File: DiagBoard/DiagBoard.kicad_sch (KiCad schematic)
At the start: 64 parts, among them J1 B1, P1 Conn_02x36_Top_Bottom, SW1 SW_DIP_x07, SW2 SW_Push, SW3 SW_DIP_x04

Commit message: DiagBoard: Elements placement
Starting PCB preliminary routing, evaluated elements placement.
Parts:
- removed C1: C, Capacitor_THT:C_Disc_D4.3mm_W1.9mm_P5.00mm, symbol Device:C
- removed SW2: SW_Push, symbol Switch:SW_Push
- removed U_B1: 74LS38, Package_DIP:DIP-14_W7.62mm, symbol 74xx:74LS38
- added C1: 150 uF 15V, Capacitor_THT:CP_Axial_L10.0mm_D4.5mm_P15.00mm_Horizontal, symbol Device:C_Polarized
- added SW2: SW_Push_DPDT, Button_Switch_THT:SW_Push_2P2T_Toggle_CK_PVA2OAH5xxxxxxV2, symbol Switch:SW_Push_DPDT
- added unit 5 of U_AB1
- C2, C3: footprint Capacitor_THT:CP_Axial_L20.0mm_D10.0mm_P26.00mm_Horizontal -> Capacitor_THT:CP_Axial_L25.0mm_D10.0mm_P30.00mm_Horizontal
- D1: footprint Diode_THT:D_5KPW_P12.70mm_Horizontal -> Diode_THT:D_5W_P10.16mm_Horizontal
- DIS1, DIS2: footprint Package_DIP:DIP-14_W7.62mm -> Package_DIP:DIP-14_W7.62mm_Socket
- R5, R6, R7: footprint (none) -> Resistor_THT:R_Axial_DIN0207_L6.3mm_D2.5mm_P10.16mm_Horizontal
- R8: footprint Resistor_THT:R_Axial_DIN0204_L3.6mm_D1.6mm_P5.08mm_Horizontal -> Resistor_THT:R_Axial_DIN0207_L6.3mm_D2.5mm_P10.16mm_Horizontal
- SW1: footprint (none) -> Button_Switch_THT:SW_DIP_SPSTx07_Piano_10.8x19.34mm_W7.62mm_P2.54mm
- SW3: footprint (none) -> Button_Switch_THT:SW_DIP_SPSTx04_Slide_9.78x12.34mm_W7.62mm_P2.54mm
- U_D2, U_E2: footprint (none) -> Package_DIP:DIP-14_W7.62mm
- U_E1: footprint Package_DIP:DIP-12_W7.62mm -> Package_DIP:DIP-16_W7.62mm
- U_F7, U_F8: footprint Package_DIP:DIP-16_W7.62mm -> Package_DIP:DIP-18_W7.62mm
- renumbered U_8A2 to U_A2, U_8A4 to U_A4, U_8A5 to U_A5, U_8A6 to U_A6, U_8B3 to U_B3
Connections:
- net +5V: now also U_AB1.14 (VCC)
- net GND: now also U_A6.1 (OEa), C1.2, SW2.1 (A), SW2.3 (C), U_AB1.7 (GND)
- net at D1.2 (A), RN2.3 (R2), U_C4.1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: now also C1.1, SW2.2 (B)
- no-connect marks 58 -> 61
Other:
- moved on the sheet: U_C4E, U_D1G

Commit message: DiagBoard: Fix messed up address line
A11+A14, A12+A13
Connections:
- net A11: no longer U_B3.5 (O2b), U_E1.12, U_E3.5 (E2), U_E4.6 (E3)
- net A12: no longer U_B3.3 (O3b), U_E1.10, U_E3.3 (A2), U_E4.3 (A2)
- new net A13: U_B3.3 (O3b), U_E1.10, U_E3.3 (A2), U_E4.3 (A2)
- new net A14: U_B3.5 (O2b), U_E1.12, U_E3.5 (E2), U_E4.6 (E3)
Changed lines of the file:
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@@
 		)
 	)
-	(label "A13"
+	(label "A12"
 		(at 577.85 198.12 0)
 		(fields_autoplaced yes)
@@
 		)
 	)
-	(label "A14"
+	(label "A11"
 		(at 577.85 195.58 0)
 		(fields_autoplaced yes)
@@
 		)
 	)
-	(label "A11"
+	(label "A14"
 		(at 577.85 203.2 0)
 		(fields_autoplaced yes)
@@
 		)
 	)
-	(label "A12"
+	(label "A13"
 		(at 577.85 200.66 0)
 		(fields_autoplaced yes)

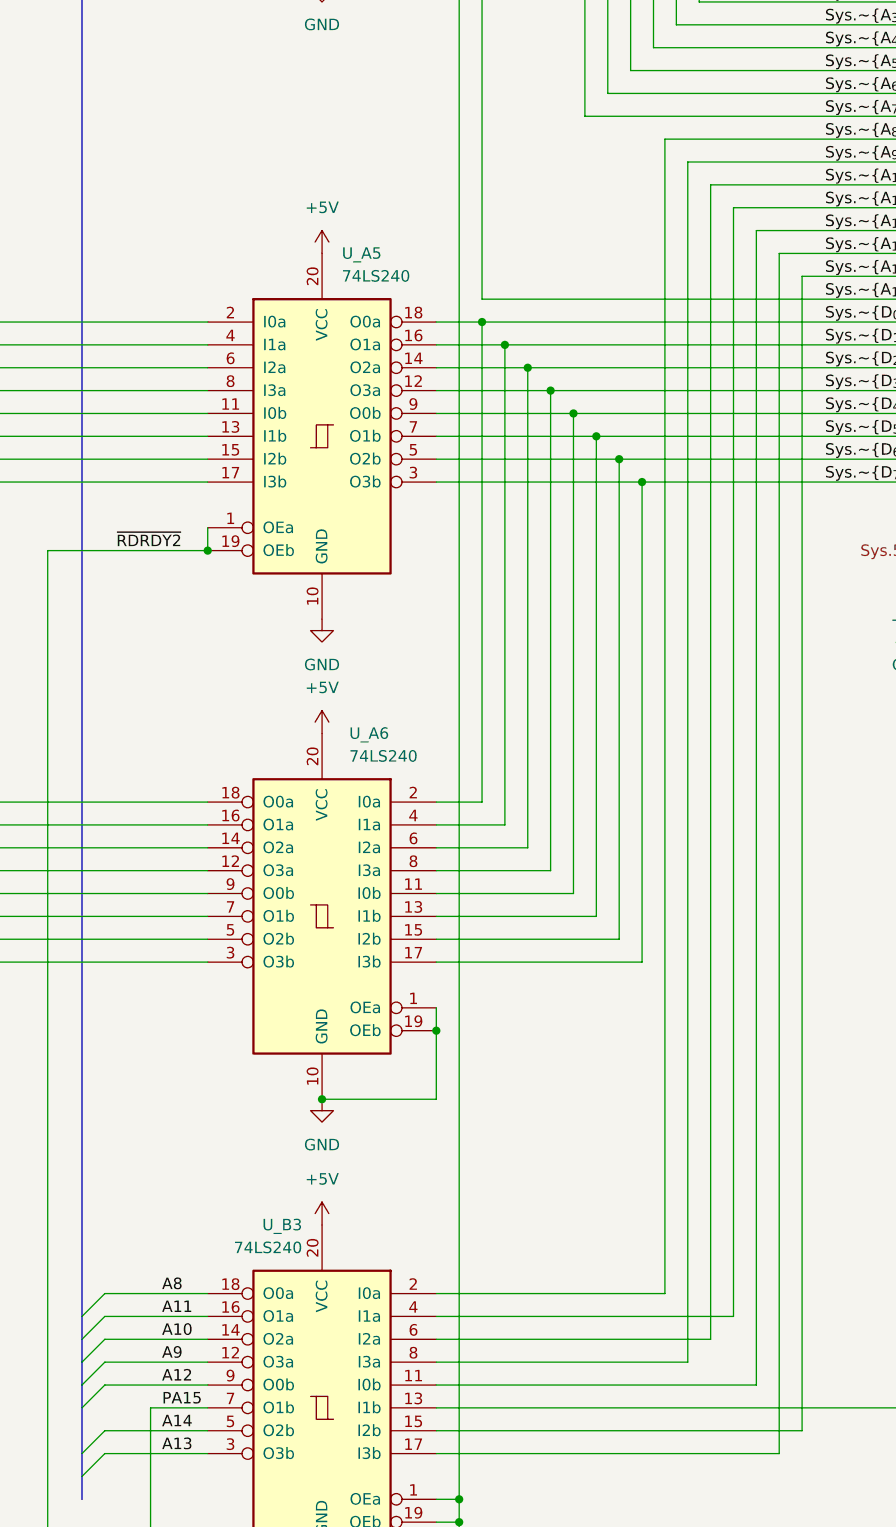
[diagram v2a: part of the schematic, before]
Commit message: DiagBoard: Untwist U_B3 lines
Routes easier
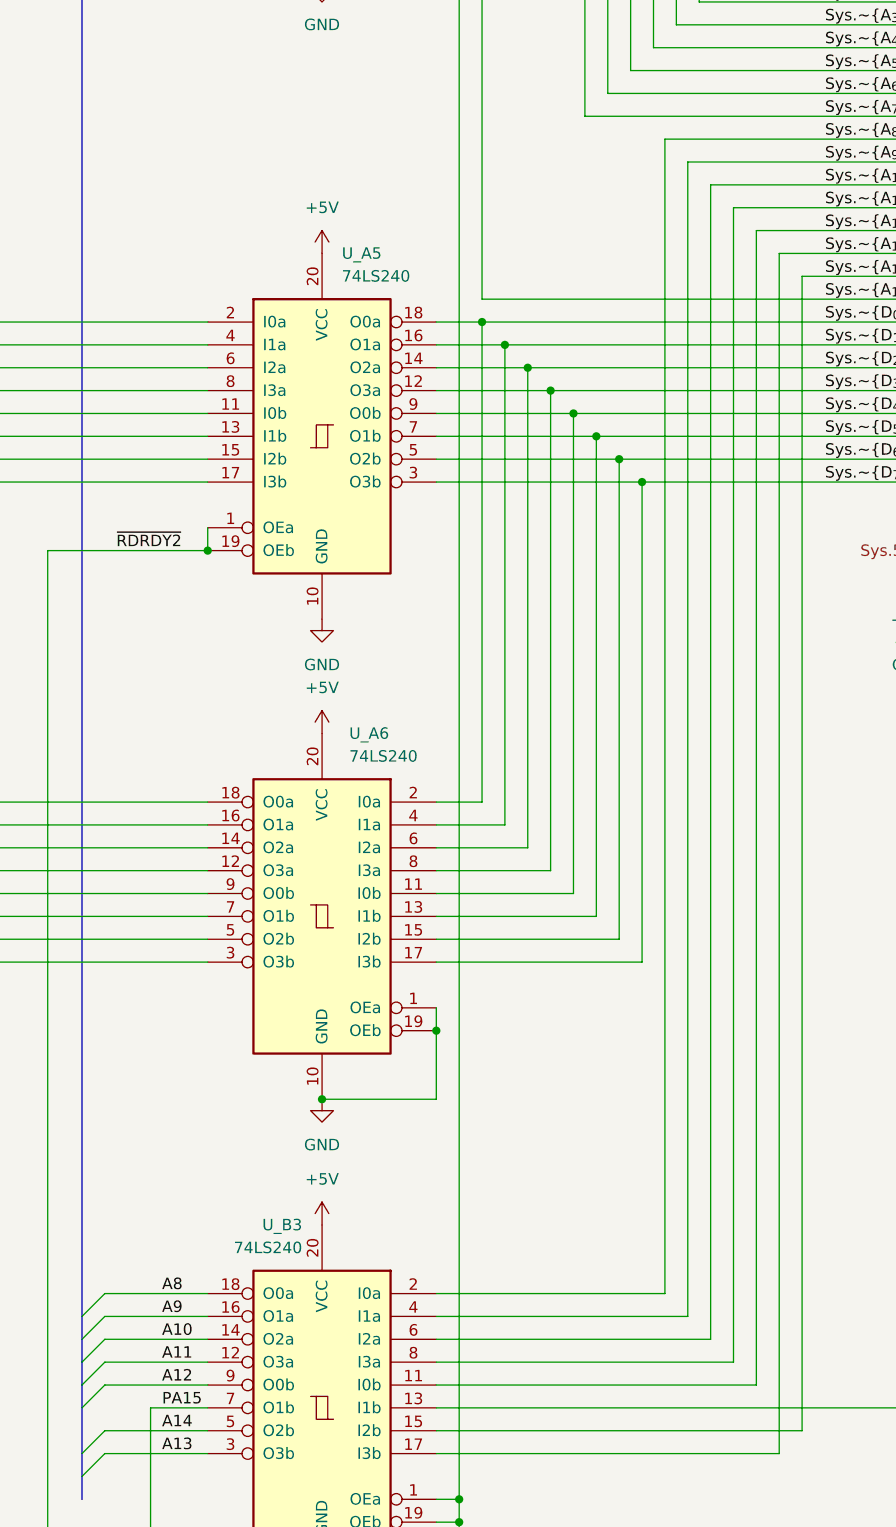
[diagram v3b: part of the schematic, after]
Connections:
- net A11: now also U_B3.12 (O3a); no longer U_B3.16 (O1a)
- net A9: now also U_B3.16 (O1a); no longer U_B3.12 (O3a)
- net Sys.~{A_{11}}: now also U_B3.8 (I3a); no longer U_B3.4 (I1a)
- net Sys.~{A_{9}}: now also U_B3.4 (I1a); no longer U_B3.8 (I3a)
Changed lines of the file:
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@@
 	(wire
 		(pts
+			(xy 623.57 405.13) (xy 651.51 405.13)
+		)
+		(stroke
+			(width 0)
+			(type default)
+		)
+	)
+	(wire
+		(pts
 			(xy 664.21 510.54) (xy 664.21 554.99)
 		)
@@
 	(wire
 		(pts
+			(xy 651.51 405.13) (xy 651.51 276.86)
+		)
+		(stroke
+			(width 0)
+			(type default)
+		)
+	)
+	(wire
+		(pts
 			(xy 254 452.12) (xy 264.16 452.12)
 		)
@@
 	(wire
 		(pts
-			(xy 623.57 405.13) (xy 656.59 405.13)
-		)
-		(stroke
-			(width 0)
-			(type default)
-		)
-	)
-	(wire
-		(pts
 			(xy 269.24 445.77) (xy 273.05 445.77)
 		)
@@
 	(wire
 		(pts
+			(xy 623.57 407.67) (xy 654.05 407.67)
+		)
+		(stroke
+			(width 0)
+			(type default)
+		)
+	)
+	(wire
+		(pts
 			(xy 82.55 228.6) (xy 72.39 228.6)
 		)
@@
 	(wire
 		(pts
-			(xy 623.57 410.21) (xy 651.51 410.21)
-		)
-		(stroke
-			(width 0)
-			(type default)
-		)
-	)
-	(wire
-		(pts
 			(xy 261.62 464.82) (xy 261.62 533.4)
 		)
@@
 		)
 	)
-	(wire
-		(pts
-			(xy 651.51 410.21) (xy 651.51 276.86)
-		)
-		(stroke
-			(width 0)
-			(type default)
-		)
-	)
 	(bus
 		(pts
@@
 	(wire
 		(pts
-			(xy 623.57 407.67) (xy 654.05 407.67)
-		)
-		(stroke
-			(width 0)
-			(type default)
-		)
-	)
-	(wire
-		(pts
 			(xy 322.58 209.55) (xy 322.58 172.72)
 		)
@@
 	(wire
 		(pts
-			(xy 656.59 405.13) (xy 656.59 281.94)
+			(xy 656.59 281.94) (xy 656.59 410.21)
 		)
 		(stroke
@@
 	(wire
 		(pts
+			(xy 623.57 410.21) (xy 656.59 410.21)
+		)
+		(stroke
+			(width 0)
+			(type default)
+		)
+	)
+	(wire
+		(pts
 			(xy 353.06 193.04) (xy 356.87 193.04)
 		)
@@
 		)
 	)
-	(label "A9"
+	(label "A11"
 		(at 593.09 410.21 0)
 		(fields_autoplaced yes)
@@
 		)
 	)
-	(label "A11"
+	(label "A9"
 		(at 593.09 405.13 0)
 		(fields_autoplaced yes)

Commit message: DiagBoard: Layout in progress
WIP dump. SRAM chips need replacement.
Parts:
- added unit 5 of U_C1
- added unit 2 of U_C1
- added unit 4 of U_C1
- added unit 3 of U_C1
- added unit 3 of U_E1
- U_E1: footprint Package_DIP:DIP-16_W7.62mm -> Package_DIP:DIP-14_W7.62mm
- renumbered U_X1 to U_C1
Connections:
- net +5V: now also U_C1.14 (VCC), U_E1.14 (VCC)
- net D0_O: now also RN1.5 (R4); no longer RN1.3 (R2)
- net D2_O: now also RN1.4 (R3); no longer RN1.8 (R7)
- net D3_O: now also RN1.3 (R2); no longer RN1.9 (R8)
- net D5_O: now also RN1.8 (R7); no longer RN1.6 (R5)
- net D6_O: now also RN1.9 (R8); no longer RN1.5 (R4)
- net D7_O: now also RN1.6 (R5); no longer RN1.4 (R3)
- net GND: now also U_C1.7 (GND), U_E1.7 (GND)
- net at SW1.10, U_K7.14 (D5): now also RN2.7 (R6); no longer RN2.8 (R7)
- net at SW1.11, U_K7.13 (D4): now also RN2.6 (R5); no longer RN2.7 (R6)
- net at SW1.12, U_K7.3 (D0): now also RN2.5 (R4); no longer RN2.6 (R5)
- net at SW1.13, U_K7.4 (D1): now also RN2.4 (R3); no longer RN2.5 (R4)
- net at SW1.14, U_K7.7 (D2): now also RN2.3 (R2); no longer RN2.4 (R3)
- net at SW1.8, U_K7.18 (D7): now also RN2.9 (R8); no longer RN2.10 (R9)
- net at SW1.9, U_K7.17 (D6): now also RN2.8 (R7); no longer RN2.9 (R8)
- net at RN2.2 (R1): now also C1.1, D1.2 (A), SW2.2 (B), U_C4.1, U_C4.2
- no-connect marks 61 -> 70
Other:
- moved on the sheet: C2, C3

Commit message: DiagBoard: Signals layout complete
No power and ground yet. Fixed U_A2 type
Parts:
- U_A2: symbol 74xx:74LS244 -> 74xx:74LS240
- U_F7, U_F8: footprint Package_DIP:DIP-18_W7.62mm -> ExtraFootprints:DIP-18_W10.16mm
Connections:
- net D2: now also U_F8.12 (Q2); no longer U_F8.11 (Q2)
- net D3: now also U_F8.11 (Q3); no longer U_F8.9 (GND)
- net D4: now also U_F7.11 (Q3); no longer U_F7.9 (GND)
- net D5: now also U_F7.12 (Q2); no longer U_F7.11 (Q2)

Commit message: DiagBoard: Complete reconstruction
Complete with extra functionality and connectors for experiments
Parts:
- removed J1: B1, Connector_Wire:SolderWire-0.1sqmm_1x01_D0.4mm_OD1mm, symbol Connector:Conn_01x01_Pin
- added C10, C11, C12, C13, C14, C15, C16, C17, C18, C19, C20, C21, C22, C23, C24, C25, C26, C27, C29, C30, C31, C4, C5, C6, C7, C8, C9: 100n, Capacitor_THT:C_Disc_D4.3mm_W1.9mm_P5.00mm, symbol Device:C
- added C28: 100n, Capacitor_THT:C_Rect_L9.0mm_W2.5mm_P7.50mm_MKT, symbol Device:C
- added J1: WR RD, Connector_PinHeader_2.54mm:PinHeader_1x02_P2.54mm_Vertical, symbol Connector:Conn_01x02_Pin
- added J11: Data bus, Connector_IDC:IDC-Header_2x08_P2.54mm_Vertical, symbol Connector_Generic:Conn_02x08_Odd_Even
- added J12: A7 B1, Connector_PinHeader_2.54mm:PinHeader_1x02_P2.54mm_Vertical, symbol Connector:Conn_01x02_Pin
- added J2: Voltage test port, Connector_Wago:Wago_734-134_1x04_P3.50mm_Vertical, symbol Connector:Conn_01x04_Pin
- added J3: CLK, Connector_PinHeader_2.54mm:PinHeader_1x01_P2.54mm_Vertical, symbol Connector:Conn_01x01_Pin
- added J4: INR CPL, Connector_PinHeader_2.54mm:PinHeader_1x08_P2.54mm_Vertical, symbol Connector:Conn_01x08_Pin
- added J5: D5 E8, Connector_PinHeader_2.54mm:PinHeader_1x02_P2.54mm_Vertical, symbol Connector:Conn_01x02_Pin
- added J6: External control, Connector_PinSocket_2.54mm:PinSocket_1x05_P2.54mm_Vertical, symbol Connector:Conn_01x05_Pin
- added J7: Conn_01x03_Pin, Connector_PinHeader_2.54mm:PinHeader_1x03_P2.54mm_Vertical, symbol Connector:Conn_01x03_Pin
- added J8: J3 E6 D6 D7, Connector_PinHeader_2.54mm:PinHeader_1x04_P2.54mm_Vertical, symbol Connector:Conn_01x04_Pin
- added J9: Address bus, Connector_IDC:IDC-Header_2x20_P2.54mm_Vertical, symbol Connector_Generic:Conn_02x20_Odd_Even
- added U_A3, U_B4: 74LS244, Package_DIP:DIP-20_W7.62mm, symbol 74xx:74LS240
- added unit 4 of U_D1
- added unit 5 of U_D1
- added unit 4 of U_J5
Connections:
- net +12V: now also J2.1 (Pin_1)
- net +5V: now also C10.1, C11.1, C12.1, C13.1, C14.1, C15.1, C16.1, C17.1, C18.1, C19.1, C20.1, C21.1, C22.1, C23.1, C24.1, C25.1, C26.1, C27.1, C28.1, C29.1, C30.1, C31.1, C4.1, C5.1, C6.1, C7.1, C8.1, C9.1, J2.3 (Pin_3), J9.37 (Pin_37), J9.38 (Pin_38), J9.39 (Pin_39), J9.40 (Pin_40), U_A3.20 (VCC), U_B4.20 (VCC), U_J5.14 (VCC)
- net -12V: now also J2.4 (Pin_4); no longer P1.34 (Pin_34), P1.70 (Pin_70)
- net A0: now also J9.2 (Pin_2), U_A3.2 (I0a)
- net A1: now also J9.4 (Pin_4), U_A3.4 (I1a)
- net A10: now also J9.22 (Pin_22), U_B4.6 (I2a)
- net A11: now also J9.24 (Pin_24), U_B4.8 (I3a)
- net A12: now also J9.26 (Pin_26), U_B4.11 (I0b)
- net A13: now also J9.28 (Pin_28), U_B4.17 (I3b)
- net A14: now also J9.30 (Pin_30), U_B4.15 (I2b)
- net A2: now also J9.6 (Pin_6), U_A3.6 (I2a)
- net A3: now also J9.8 (Pin_8), U_A3.8 (I3a)
- net A4: now also J9.10 (Pin_10), U_A3.11 (I0b)
- net A5: now also J9.12 (Pin_12), U_A3.13 (I1b)
- net A6: now also J9.14 (Pin_14), U_A3.15 (I2b)
- net A7: now also J9.16 (Pin_16), U_A3.17 (I3b)
- net A8: now also J9.18 (Pin_18), U_B4.2 (I0a)
- net A9: now also J9.20 (Pin_20), U_B4.4 (I1a)
- net BUSRD: now also U_B5.1 (OE), U_J7.9 (Zc); no longer U_B5.11 (LE), U_J7.7 (Zb)
- net D0_O: now also J11.2 (Pin_2)
- net D1_O: now also J11.4 (Pin_4)
- net D2_O: now also J11.6 (Pin_6)
- net D3_O: now also J11.8 (Pin_8)
- net D4_O: now also J11.10 (Pin_10)
- net D5_O: now also J11.12 (Pin_12)
- net D6_O: now also J11.14 (Pin_14)
- net D7_O: now also J11.16 (Pin_16)
- net GND: now also C10.2, C11.2, C12.2, C13.2, C14.2, C15.2, C16.2, C17.2, C18.2, C19.2, C20.2, C21.2, C22.2, C23.2, C24.2, C25.2, C26.2, C27.2, C28.2, C29.2, C30.2, C31.2, C4.2, C5.2, C6.2, C7.2, C8.2, C9.2, J11.1 (Pin_1), J11.11 (Pin_11), J11.13 (Pin_13), J11.15 (Pin_15), J11.3 (Pin_3), J11.5 (Pin_5), J11.7 (Pin_7), J11.9 (Pin_9), J2.2 (Pin_2), J9.1 (Pin_1), J9.11 (Pin_11), J9.13 (Pin_13), J9.15 (Pin_15), J9.17 (Pin_17), J9.19 (Pin_19), J9.21 (Pin_21), J9.23 (Pin_23), J9.25 (Pin_25), J9.27 (Pin_27), J9.29 (Pin_29), J9.3 (Pin_3), J9.31 (Pin_31), J9.33 (Pin_33), J9.35 (Pin_35), J9.5 (Pin_5), J9.7 (Pin_7), J9.9 (Pin_9), U_A3.10 (GND), U_B4.10 (GND), U_J5.7 (GND); no longer SW2.1 (A)
- net HIGH: now also U_A4.19 (OEb), J6.5 (Pin_5), U_A3.1 (OEa), U_A3.19 (OEb), U_B4.1 (OEa), U_B4.19 (OEb)
- net HIGHMEM: now also U_A4.11 (I0b)
- net LOW: no longer U_A4.19 (OEb)
- net PA15: now also J9.32 (Pin_32), U_B4.13 (I1b)
- net PA16: now also U_A4.13 (I1b), J9.34 (Pin_34)
- net PA17: now also U_A4.15 (I2b), J9.36 (Pin_36)
- net Sys.~{A_{0}}: now also U_A3.18 (O0a)
- net Sys.~{A_{10}}: now also U_B4.14 (O2a)
- net Sys.~{A_{11}}: now also U_B4.12 (O3a)
- net Sys.~{A_{12}}: now also U_B4.9 (O0b)
- net Sys.~{A_{13}}: now also U_B4.3 (O3b)
- net Sys.~{A_{14}}: now also U_B4.5 (O2b)
- net Sys.~{A_{15}}: now also U_A4.9 (O0b)
- net Sys.~{A_{1}}: now also U_A3.16 (O1a)
- net Sys.~{A_{2}}: now also U_A3.14 (O2a)
- net Sys.~{A_{3}}: now also U_A3.12 (O3a)
- net Sys.~{A_{4}}: now also U_A3.9 (O0b)
- net Sys.~{A_{5}}: now also U_A3.7 (O1b)
- net Sys.~{A_{6}}: now also U_A3.5 (O2b)
- net Sys.~{A_{7}}: now also U_A3.3 (O3b)
- net Sys.~{A_{8}}: now also U_B4.18 (O0a)
- net Sys.~{A_{9}}: now also U_B4.16 (O1a)
- net Sys.~{CPL_{0}}: now also J4.5 (Pin_5)
- net Sys.~{CPL_{1}}: now also J4.6 (Pin_6)
- net Sys.~{CPL_{2}}: now also J4.7 (Pin_7)
- net Sys.~{CPL_{3}}: now also J4.8 (Pin_8)
- net Sys.~{DRDY}: now also U_D1.11
- net Sys.~{INR_{0}}: now also J4.4 (Pin_4)
- net Sys.~{INR_{1}}: now also J4.1 (Pin_1)
- net Sys.~{INR_{2}}: now also J4.2 (Pin_2)
- net Sys.~{INR_{3}}: now also J4.3 (Pin_3)
- net Sys.~{INTACK}: now also J7.3 (Pin_3)
- net Sys.~{INTRQ}: now also J7.1 (Pin_1)
- net Sys.~{MEMFLT}: now also J7.2 (Pin_2)
- net Sys.~{PA_{15}}: now also U_B4.7 (O1b)
- net Sys.~{PA_{16}}: now also U_A4.7 (O1b)
- net Sys.~{PA_{17}}: now also U_A4.5 (O2b)
- net Ext.BUSRD: now reaches U_J7.11 (I0c)
- net Ext.BUSRD: now also J6.2 (Pin_2)
- net Ext.~{MEMSEL}: now reaches U_J6.6, U_J7.14 (I0d)
- net Ext.~{D_OUT}: now reaches U_J5.8, U_J7.2 (I0a)
- net DIAGRD: now reaches U_E7.1 (A->B), U_H8.1 (Ea1), U_J8.7 (Zb)
- net at U_J6.4: now also J8.4 (Pin_4)
- net at U_AB1.13: now also J1.2 (Pin_2)
- net Ext.DIAGRD: now reaches U_J5.3, U_J8.5 (I0b)
- net Ext.DIAGRD: now also J6.1 (Pin_1)
- net at U_J5.11, U_J5.4: now also J8.3 (Pin_3)
- net at U_J5.6: now also J8.1 (Pin_1)
- net at U_C4.12: now also J5.1 (Pin_1)
- net at U_C4.13: now also J5.2 (Pin_2)
- net at U_J5.10: now also J8.2 (Pin_2)
- net Ext.~{MMIO}: now reaches U_J8.11 (I0c)
- net Ext.~{MMIO}: now also J6.3 (Pin_3)
- net Ext.~{DIAGWR}: now reaches U_J8.2 (I0a)
- net Ext.~{DIAGWR}: now also J6.4 (Pin_4)
- net at SW3.4: now also J3.1 (Pin_1)
- net NC_B1 renamed Ext.RDIN
- net Ext.RDIN: now also J1.1 (Pin_1)
- net ~{RDRDY2} renamed ~{Sys.D_OUT}
- new net: J12.1 (Pin_1), U_D1.8
- new net: J12.2 (Pin_2), U_D1.10, U_D1.9
- new net BUSWR_LE: U_B5.11 (LE), U_J7.7 (Zb)
- no-connect marks 70 -> 67
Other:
- note added: "Data write gate (CPU to card) LE is hardwired to 1 via U_J7 ~{OE} goes low when the CPU is writing to the card"
- note added: "These two MUXes are hardwired to pass B input. Looks like some incomplete/unimplemented functionality"
- note removed: "Data write gate (CPU to card)"
- note removed: "These two MUXes are hardwared to pass B input. Looks like some incomplete/unimplemented functionality"
- moved on the sheet: C2, C3, P1, R8, RN1, U_A1B, U_A1C, U_A1E, U_A2, U_A4, U_A5, U_A6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

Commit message: DiagBoard, MUX: Verified space for puller tabs
Board layouts allow for two tabs, reserve space for both. Removed pre-defined
holes because tabs can be different depending on where they were ordered, it's
easier to drill two custom holes on the spot
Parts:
- J1, J11, J12, J4, J5, J6, J7, J8, J9, U_A3, U_B4: now not fitted
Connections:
- net GND: now also SW2.6 (C)
- no-connect marks 67 -> 66
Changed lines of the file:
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@@
 	)
 	(junction
+		(at 34.29 218.44)
+		(diameter 0)
+		(color 0 0 0 0)
+	)
+	(junction
 		(at 167.64 199.39)
 		(diameter 0)
@@
 	)
 	(no_connect
-		(at 36.83 218.44)
-	)
-	(no_connect
 		(at 711.2 322.58)
 	)
@@
 		)
 	)
+	(wire
+		(pts
+			(xy 34.29 218.44) (xy 34.29 226.06)
+		)
+		(stroke
+			(width 0)
+			(type default)
+		)
+	)
 	(bus
 		(pts
@@
 		)
 	)
+	(wire
+		(pts
+			(xy 34.29 218.44) (xy 36.83 218.44)
+		)
+		(stroke
+			(width 0)
+			(type default)
+		)
+	)
 	(bus
 		(pts
@@
 	(wire
 		(pts
-			(xy 34.29 208.28) (xy 34.29 226.06)
+			(xy 34.29 208.28) (xy 34.29 218.44)
 		)
 		(stroke
@@
 		(in_bom yes)
 		(on_board yes)
-		(dnp no)
+		(dnp yes)
 		(property "Reference" "U_B4"
 			(at 642.2233 448.31 0)
@@
 		(in_bom yes)
 		(on_board yes)
-		(dnp no)
+		(dnp yes)
 		(fields_autoplaced yes)
 		(property "Reference" "J8"
@@
 		(in_bom yes)
 		(on_board yes)
-		(dnp no)
+		(dnp yes)
 		(fields_autoplaced yes)
 		(property "Reference" "J9"
@@
 		(in_bom yes)
 		(on_board yes)
-		(dnp no)
+		(dnp yes)
 		(fields_autoplaced yes)
 		(property "Reference" "J7"
@@
 		(in_bom yes)
 		(on_board yes)
-		(dnp no)
+		(dnp yes)
 		(property "Reference" "J6"
 			(at 175.895 170.18 0)
@@
 		(in_bom yes)
 		(on_board yes)
-		(dnp no)
+		(dnp yes)
 		(property "Reference" "U_A3"
 			(at 640.9533 152.4 0)
@@
 		(in_bom yes)
 		(on_board yes)
-		(dnp no)
+		(dnp yes)
 		(fields_autoplaced yes)
 		(property "Reference" "J11"
@@
 		(in_bom yes)
 		(on_board yes)
-		(dnp no)
+		(dnp yes)
 		(fields_autoplaced yes)
 		(property "Reference" "J1"
@@
 		(in_bom yes)
 		(on_board yes)
-		(dnp no)
+		(dnp yes)
 		(fields_autoplaced yes)
 		(property "Reference" "J4"
@@
 		(in_bom yes)
 		(on_board yes)
-		(dnp no)
+		(dnp yes)
 		(fields_autoplaced yes)
 		(property "Reference" "J5"
@@
 		(in_bom yes)
 		(on_board yes)
-		(dnp no)
+		(dnp yes)
 		(fields_autoplaced yes)
 		(property "Reference" "J12"

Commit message: DiagBoard: Add memory delay selection jumper
For experiments and fine-tuning.
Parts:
- added JP1: Memory delay select, Connector_PinHeader_2.54mm:PinHeader_2x08_P2.54mm_Vertical, symbol Jumper:Jumper_2_Bridged
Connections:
- net DRDY: now also JP1.10 (B5), JP1.12 (B6), JP1.14 (B7), JP1.16 (B8), JP1.2 (B1), JP1.4 (B2), JP1.6 (B3), JP1.8 (B4); no longer U_E2.5 (Qc)
- net SR1: now also JP1.1 (A1)
- net at U_E2.10 (Qe): now also JP1.9 (A5)
- net at U_E2.11 (Qf): now also JP1.11 (A6)
- net at U_E2.12 (Qg): now also JP1.13 (A7)
- net at U_E2.13 (Qh): now also JP1.15 (A8)
- net at U_E2.4 (Qb): now also JP1.3 (A2)
- net at U_E2.6 (Qd): now also JP1.7 (A4)
- new net: JP1.5 (A3), U_E2.5 (Qc)
- no-connect marks 66 -> 59
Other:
- moved on the sheet: U_C8D, U_E2, U_J4D, U_J5A
